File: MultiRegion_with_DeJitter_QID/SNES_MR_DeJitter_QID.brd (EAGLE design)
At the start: 85.2 x 26.4 mm, 80 parts, among them J1 SNESCART_CONN_SPARSE_4, Q31 2SC2412, U1 SuperCIC_lock, U2 uIGR, U3 EPM7032AETC44-10N, U4 74HCT2G125DP, U5 CDCE913, U6 2G17TI_DBV, U7 TLV70033, U8 TLV70018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

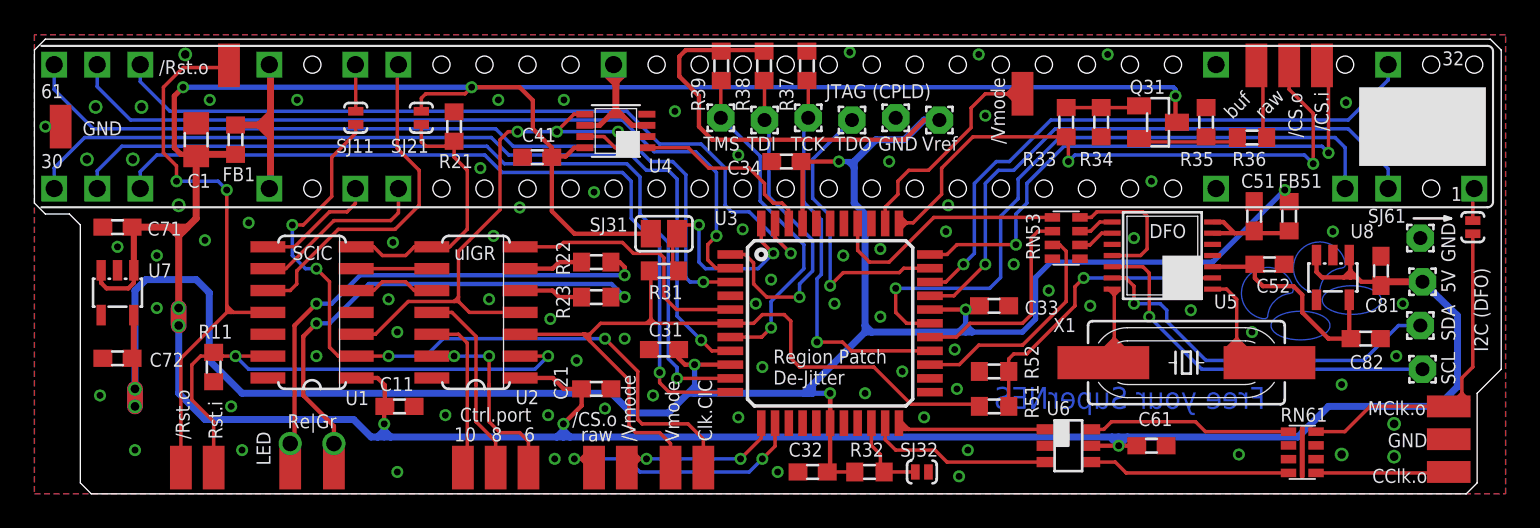
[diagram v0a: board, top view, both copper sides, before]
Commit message: PCB update: - double /CS.i pad - color carrier generate inside CPLD (trace removed) - replace resistor arrays by simple components - add footprint for resistor from SNES mainboard to have resistor not loosely connected
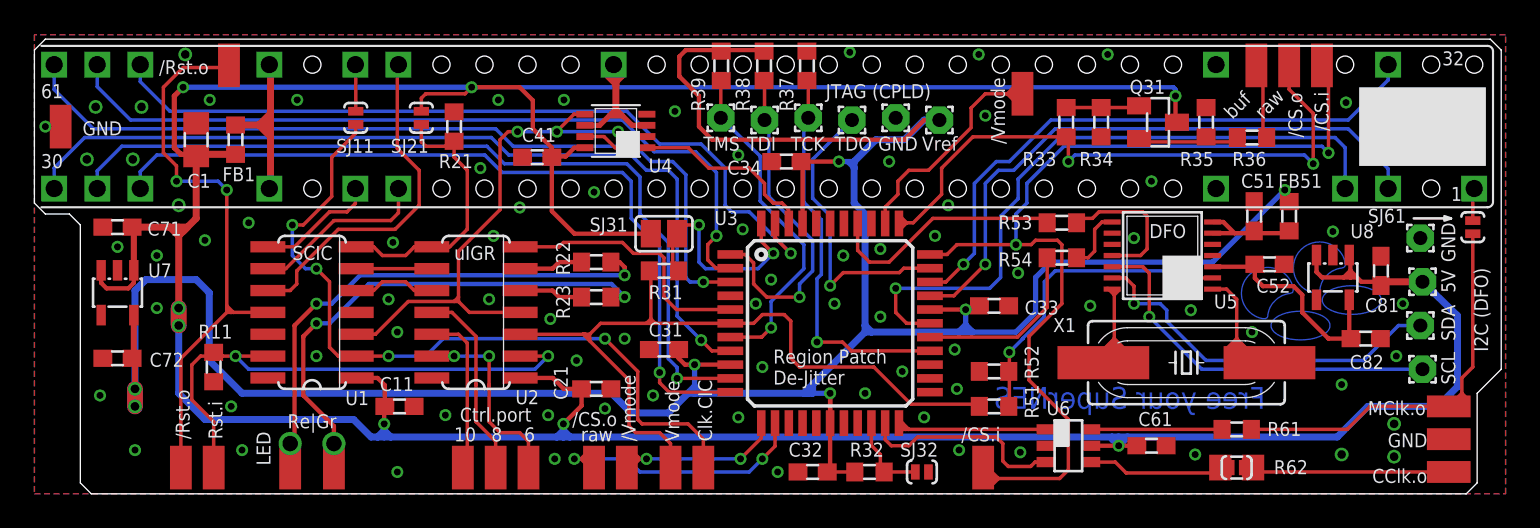
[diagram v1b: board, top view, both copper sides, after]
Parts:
- removed RN53, RN61: CAY16-39R0F4LF, resistor-net:CTS742C083
- added CSYNC_I1: (no value), wirepad:SMD1,27-2,54
- added R53, R54, R61: 39, rcl:R0603
- added R62: from SNES-MB, rcl:R0805
- added SJ62: (no value), jumper:SJ_SMALL
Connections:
- removed net COLOR_SC_NTSC_PRE: RN53.3, U5.8
- removed net COLOR_SC_PAL: RN53.7, U3.25
- removed net COLOR_SC_PAL_PRE: RN53.2, U5.9
- new net MCLK_PAL_EXT_I_PRE: R54.1, U5.8
- net COLOR_SC_O: now also R62.2, SJ62.2; no longer RN61.5
- net COLOR_SC_O_PRE: now also R62.1, SJ62.1; no longer RN61.4
- net CSYNC_I: now also CSYNC_I1.1
- net GND: no longer RN53.1, RN53.8, RN61.2, RN61.3, RN61.6, RN61.7
- net MCLK_BASE_I: now also R53.2; no longer RN53.5
- net MCLK_BASE_I_PRE: now also R53.1; no longer RN53.4
- net MCLK_EXT_O: now also R61.2; no longer RN61.8
- net MCLK_EXT_O_PRE: now also R61.1; no longer RN61.1
- net MCLK_PAL_EXT_I: now also R54.2; no longer RN53.6
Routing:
- net CSYNC_I: track 32.9 -> 58.2 mm
- net COLOR_SC_PAL: track 13.3 -> 0.00 mm
- net COLOR_SC_O: track 7.73 -> 12.0 mm
- net MCLK_EXT_O_PRE: track 11.9 -> 7.63 mm
- net MCLK_EXT_O: track 20.5 -> 24.2 mm
- net MCLK_PAL_EXT_I_PRE: track 0.00 -> 3.68 mm
- net COLOR_SC_O_PRE: track 11.8 -> 8.49 mm
- net GND: track 2.79 -> 0.00 mm, vias 81 -> 80
- net COLOR_SC_PAL_PRE: track 2.15 -> 0.00 mm
- net COLOR_SC_NTSC_PRE: track 2.09 -> 0.00 mm
- net MCLK_PAL_EXT_I: track 12.3 -> 10.4 mm
- net COLOR_SC_PRE: track 10.8 -> 12.1 mm
- net PALMODE.1V8: track 17.2 -> 18.4 mm
- net +3V3: track 162.7 -> 162.1 mm
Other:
- board text added: "SMR20190813"
- board text removed: "SMR20190603"

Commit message: update PCB design: - selectable sync level for the buffered output - video buffer for sync instead of transistor
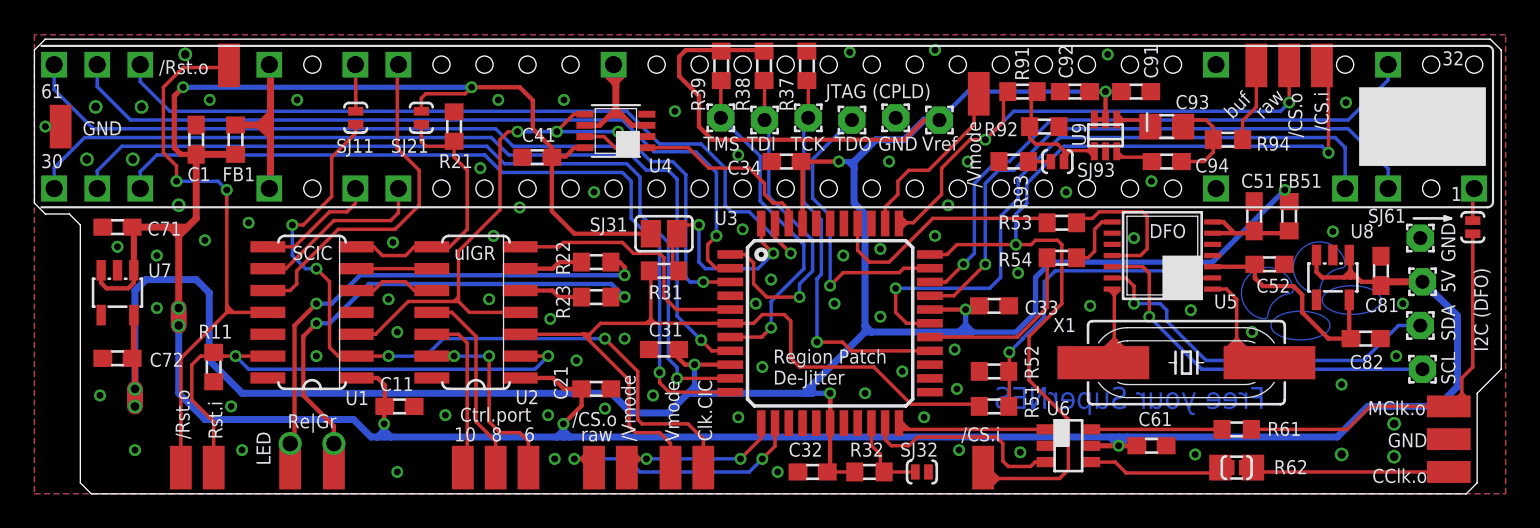
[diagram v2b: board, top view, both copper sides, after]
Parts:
- removed Q31: 2SC2412, transistor:SOT23-BEC
- removed R33: 1k, rcl:R0603
- removed R34: 10k, rcl:R0603
- removed R35: 300, rcl:R0603
- removed R36: 100, rcl:R0603
- added C91: 10u, rcl:C0603
- added C92: 0.01u, rcl:C0603
- added C93: 33u, rcl:C0805
- added C94: 22u, rcl:C0603
- added R91: 4k7, rcl:R0603
- added R92: 2k, rcl:R0603
- added R93: 623, rcl:R0603
- added R94: 75, rcl:R0603
- added SJ93: (no value), jumper:SJ_SMALL
- added U9: TSH122ICT, st-microelectronics:SC70
- C1: device rcl:C0805 -> rcl:C0603
- moved #PALMODE_1 2.54 mm to (54.9, 23.2)
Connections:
- removed net CSYNC_O_POST_Q: Q31.E, R35.1, R36.1
- removed net CSYNC_O_PRE_Q: Q31.B, R33.1, R34.1
- new net N$1: R91.2, R92.1, SJ93.1, U9.P$1
- new net N$10: R93.1, SJ93.2
- new net N$7: C94.1, U9.P$3
- new net N$8: C93.1, U9.P$4
- new net N$9: C93.2, C94.2, R94.1
- net +3V3: now also C91.1, C92.1, U9.P$5, U9.P$6
- net +5V: no longer Q31.C
- net CSYNC_O: now also R94.2; no longer R36.2
- net CSYNC_O_3V3_1: now also R91.1; no longer R33.2
- net GND: now also C91.2, C92.2, R92.2, R93.2, U9.P$2; no longer R34.2, R35.2
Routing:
- net +5V: track 229.8 -> 187.3 mm, vias 8 -> 7
- net +3V3: track 162.1 -> 177.0 mm, vias 7 -> 8
- net N$1: track 0.00 -> 10.1 mm
- net CSYNC_O_POST_Q: track 6.22 -> 0.00 mm
- net N$9: track 0.00 -> 5.62 mm
- net CSYNC_O_PRE_Q: track 4.28 -> 0.00 mm
- net NPALMODE_1: track 14.7 -> 10.8 mm
- net N$8: track 0.00 -> 3.21 mm
- net CSYNC_O_3V3_1: track 36.1 -> 33.0 mm
- net N$7: track 0.00 -> 2.66 mm
- net N$10: track 0.00 -> 1.31 mm
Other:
- board text added: "Info: - Schematic and PCB design (c) 2019 - 2020 by Peter Bartmann - Design uses De-Jitter design (c) 2017-2018 by Markus Hiienkari - Design uses DFO 5V design by micro (2015)"
- board text added: "SMR20200323"
- board text removed: "Info: - Schematic and PCB design (c) 2019 by Peter Bartmann - Design uses De-Jitter design (c) 2017-2018 by Markus Hiienkari - Design uses DFO 5V design by micro (2015)"
- board text removed: "SMR20190813"
